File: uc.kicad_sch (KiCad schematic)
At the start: 18 parts, among them J5 490107670612, SW1 DSHP08TSGET, SW2 FSMH, U2 STM32L432KCUx, U8 AD7747, Y1 ECS-.327-7-12RR-TR

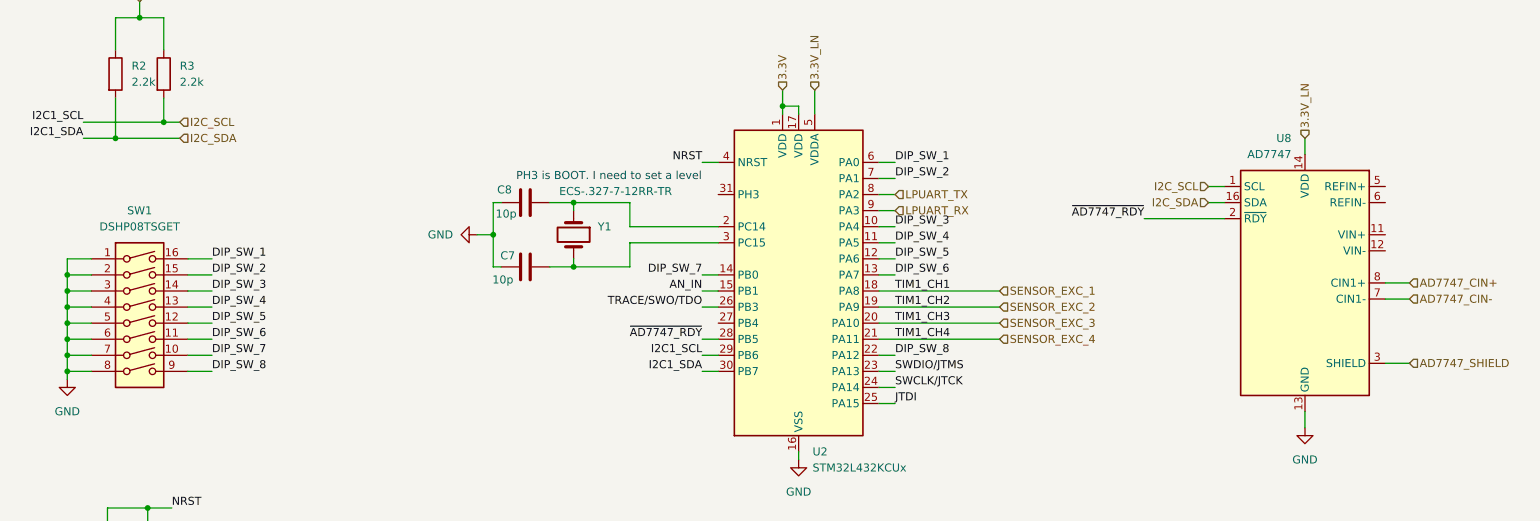
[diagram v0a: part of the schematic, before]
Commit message: rule-check: Fix the ERC errors and warnings
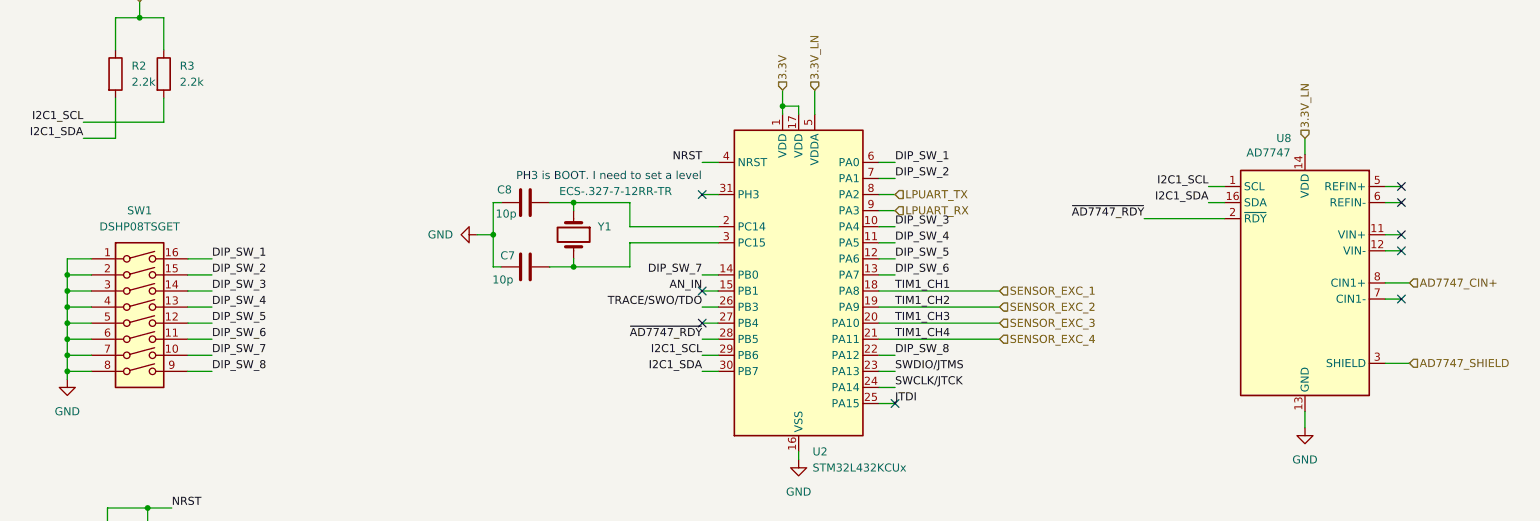
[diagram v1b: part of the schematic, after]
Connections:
- net AD7747_CIN-: no longer names the net of U8.7 (CIN1-)
- net I2C_SCL renamed I2C1_SCL
- net I2C_SDA renamed I2C1_SDA
- no-connect marks 0 -> 9
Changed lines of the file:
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@@
 	)
 	(junction
-		(at 38.1 72.39)
-		(diameter 0)
-		(color 0 0 0 0)
-	)
-	(junction
 		(at 102.87 95.25)
 		(diameter 0)
@@
 	)
 	(junction
-		(at 30.48 74.93)
-		(diameter 0)
-		(color 0 0 0 0)
-	)
-	(junction
 		(at 135.89 69.85)
 		(diameter 0)
@@
 		(color 0 0 0 0)
 	)
+	(no_connect
+		(at 233.68 90.17)
+	)
+	(no_connect
+		(at 123.19 99.06)
+	)
+	(no_connect
+		(at 233.68 82.55)
+	)
+	(no_connect
+		(at 233.68 100.33)
+	)
+	(no_connect
+		(at 123.19 104.14)
+	)
+	(no_connect
+		(at 233.68 92.71)
+	)
+	(no_connect
+		(at 233.68 85.09)
+	)
+	(no_connect
+		(at 153.67 116.84)
+	)
+	(no_connect
+		(at 123.19 83.82)
+	)
 	(wire
 		(pts
@@
 	(wire
 		(pts
+			(xy 231.14 82.55) (xy 233.68 82.55)
+		)
+		(stroke
+			(width 0)
+			(type default)
+		)
+	)
+	(wire
+		(pts
 			(xy 92.71 25.4) (xy 105.41 25.4)
 		)
@@
 	(wire
 		(pts
-			(xy 38.1 72.39) (xy 40.64 72.39)
-		)
-		(stroke
-			(width 0)
-			(type default)
-		)
-	)
-	(wire
-		(pts
 			(xy 45.72 106.68) (xy 41.91 106.68)
 		)
@@
 	(wire
 		(pts
-			(xy 231.14 100.33) (xy 234.95 100.33)
-		)
-		(stroke
-			(width 0)
-			(type default)
-		)
-	)
-	(wire
-		(pts
 			(xy 123.19 111.76) (xy 125.73 111.76)
 		)
@@
 	(wire
 		(pts
-			(xy 30.48 74.93) (xy 40.64 74.93)
+			(xy 231.14 90.17) (xy 233.68 90.17)
 		)
 		(stroke
@@
 	(wire
 		(pts
+			(xy 231.14 85.09) (xy 233.68 85.09)
+		)
+		(stroke
+			(width 0)
+			(type default)
+		)
+	)
+	(wire
+		(pts
 			(xy 34.29 53.34) (xy 34.29 55.88)
 		)
@@
 	(wire
 		(pts
+			(xy 123.19 104.14) (xy 125.73 104.14)
+		)
+		(stroke
+			(width 0)
+			(type default)
+		)
+	)
+	(wire
+		(pts
+			(xy 231.14 92.71) (xy 233.68 92.71)
+		)
+		(stroke
+			(width 0)
+			(type default)
+		)
+	)
+	(wire
+		(pts
 			(xy 151.13 88.9) (xy 153.67 88.9)
 		)
@@
 	(wire
 		(pts
+			(xy 231.14 100.33) (xy 233.68 100.33)
+		)
+		(stroke
+			(width 0)
+			(type default)
+		)
+	)
+	(wire
+		(pts
 			(xy 26.67 104.14) (xy 22.86 104.14)
 		)
@@
 	(wire
 		(pts
+			(xy 123.19 83.82) (xy 125.73 83.82)
+		)
+		(stroke
+			(width 0)
+			(type default)
+		)
+	)
+	(wire
+		(pts
 			(xy 16.51 22.86) (xy 16.51 25.4)
 		)
@@
 		)
 	)
+	(label "I2C1_SDA"
+		(at 203.2 85.09 180)
+		(effects
+			(font
+				(size 1.27 1.27)
+			)
+			(justify right bottom)
+		)
+	)
 	(label "DIP_SW_5"
 		(at 45.72 104.14 0)
@@
 		)
 	)
+	(label "I2C1_SCL"
+		(at 203.2 82.55 180)
+		(effects
+			(font
+				(size 1.27 1.27)
+			)
+			(justify right bottom)
+		)
+	)
 	(label "DIP_SW_8"
 		(at 153.67 109.22 0)
@@
 		)
 	)
-	(hierarchical_label "I2C_SDA"
-		(shape input)
-		(at 40.64 74.93 0)
-		(effects
-			(font
-				(size 1.27 1.27)
-			)
-			(justify left)
-		)
-	)
 	(hierarchical_label "LPUART_RX"
 		(shape input)
@@
 		)
 	)
-	(hierarchical_label "I2C_SDA"
-		(shape input)
-		(at 203.2 85.09 180)
-		(effects
-			(font
-				(size 1.27 1.27)
-			)
-			(justify right)
-		)
-	)
-	(hierarchical_label "I2C_SCL"
-		(shape input)
-		(at 203.2 82.55 180)
-		(effects
-			(font
-				(size 1.27 1.27)
-			)
-			(justify right)
-		)
-	)
-	(hierarchical_label "I2C_SCL"
-		(shape input)
-		(at 40.64 72.39 0)
-		(effects
-			(font
-				(size 1.27 1.27)
-			)
-			(justify left)
-		)
-	)
 	(hierarchical_label "SENSOR_EXC_2"
 		(shape input)
@@
 		)
 	)
-	(hierarchical_label "AD7747_CIN-"
-		(shape input)
-		(at 234.95 100.33 0)
-		(effects
-			(font
-				(size 1.27 1.27)
-			)
-			(justify left)
-		)
-	)
 	(symbol
 		(lib_id "Device:C")
@@
 			)
 		)
+		(property "LCSC" ""
+			(at 138.43 99.06 0)
+			(effects
+				(font
+					(size 1.27 1.27)
+				)
+				(hide yes)
+			)
+		)
 		(pin "21"
 		)
@@
 		)
 		(property "Value" "AD7747"
-			(at 216.2967 77.47 0)
+			(at 216.154 77.216 0)
 			(effects
 				(font
@@
 			)
 		)
-		(property "Datasheet" "https://www.analog.com/media/en/technical-documentation/data-sheets/AD7745_7746.pdf"
+		(property "Datasheet" "https://www.analog.com/media/en/technical-documentation/data-sheets/ad7747.pdf"
 			(at 218.44 97.79 0)
 			(effects
@@
 			)
 		)
+		(property "LCSC" ""
+			(at 218.44 97.79 0)
+			(effects
+				(font
+					(size 1.27 1.27)
+				)
+				(hide yes)
+			)
+		)
 		(pin "10"
 		)
@@
 		(pin "14"
 		)
+		(pin "4"
+		)
 		(instances

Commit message: feature: add three led to notify the status of the device
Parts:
- added D1: KT-0805B Blue, LED_SMD:LED_0805_2012Metric, symbol Device:LED
- added D2: KT-0805R Red, LED_SMD:LED_0805_2012Metric, symbol Device:LED
- added D3: KT-0805G Green, LED_SMD:LED_0805_2012Metric, symbol Device:LED
- added R1, R4: 100, Resistor_SMD:R_0603_1608Metric, symbol Device:R
- added R5: 15, Resistor_SMD:R_0603_1608Metric, symbol Device:R
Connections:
- net GND: now also D1.1 (K), D2.1 (K), D3.1 (K)
- net LED_R: now reaches U2.27 (PB4)
- net LED_R: now also R1.2
- net AN_IN renamed LED_B
- net LED_B: now also R5.1
- net JTDI renamed LED_G
- net LED_G: now also R4.2
- new net: D2.2 (A), R1.1
- new net: D1.2 (A), R5.2
- new net: D3.2 (A), R4.1
- no-connect marks 9 -> 6
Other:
- moved on the sheet: J5

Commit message: chore: fix the naming of connectors sheet file name and the change the path of footprints
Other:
- title: (none) -> ${SHEETNAME}
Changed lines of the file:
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@@
 	(generator_version "9.0")
 	(paper "A4")
+	(title_block
+		(title "${SHEETNAME}")
+	)
 	(text "Keep close to STM32 VDD\n"
 		(exclude_from_sim no)

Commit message: chore: update project to use local footprint and symbols
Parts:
- C10, C11, C13, C14, C15, C16, C19, C7, C8, C9: footprint Capacitor_SMD:C_0603_1608Metric -> footprints:C_0603_1608Metric; symbol Device:C -> symbols:C
- D1, D2, D3: footprint LED_SMD:LED_0805_2012Metric -> footprints:LED_0805_2012Metric; symbol Device:LED -> symbols:LED
- J5: footprint el-ce:Skedd490107670612_2x06_P2.54mm_Debug -> footprints:Skedd490107670612_2x06_P2.54mm_Debug; symbol Connector:Conn_01x06_Socket -> symbols:Conn_01x06_Socket
- R1, R2, R3, R4, R5: footprint Resistor_SMD:R_0603_1608Metric -> footprints:R_0603_1608Metric; symbol Device:R -> symbols:R
- SW1: footprint Button_Switch_SMD:SW_DIP_SPSTx08_Slide_KingTek_DSHP08TJ_W5.25mm_P1.27mm_JPin -> footprints:SW_DIP_SPSTx08_Slide_KingTek_DSHP08TJ_W5.25mm_P1.27mm_JPin; symbol Switch:SW_DIP_x08 -> symbols:SW_DIP_x08
- SW2: footprint Button_Switch_SMD:SW_Tactile_SPST_NO_Straight_CK_PTS636Sx25SMTRLFS -> footprints:SW_Tactile_SPST_NO_Straight_CK_PTS636Sx25SMTRLFS; symbol Switch:SW_Push -> symbols:SW_Push
- U2: footprint Package_DFN_QFN:QFN-32-1EP_5x5mm_P0.5mm_EP3.45x3.45mm -> footprints:QFN-32-1EP_5x5mm_P0.5mm_EP3.45x3.45mm; symbol MCU_ST_STM32L4:STM32L432KCUx -> symbols:STM32L432KCUx
- U8: footprint Package_SO:TSSOP-16_4.4x5mm_P0.65mm -> footprints:TSSOP-16_4.4x5mm_P0.65mm; symbol el_ce-analog_device:AD7747 -> symbols:AD7747
- Y1: footprint Crystal:Crystal_SMD_2012-2Pin_2.0x1.2mm -> footprints:Crystal_SMD_2012-2Pin_2.0x1.2mm; symbol Device:Crystal -> symbols:Crystal
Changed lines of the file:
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@@
 	)
 	(symbol
-		(lib_id "Device:LED")
+		(lib_id "symbols:LED")
 		(at 91.44 165.1 0)
 		(unit 1)
@@
 			)
 		)
-		(property "Footprint" "LED_SMD:LED_0805_2012Metric"
+		(property "Footprint" "footprints:LED_0805_2012Metric"
 			(at 91.44 165.1 0)
 			(effects
@@
 	)
 	(symbol
-		(lib_id "Device:LED")
+		(lib_id "symbols:LED")
 		(at 91.44 153.67 0)
 		(unit 1)
@@
 			)
 		)
-		(property "Footprint" "LED_SMD:LED_0805_2012Metric"
+		(property "Footprint" "footprints:LED_0805_2012Metric"
 			(at 91.44 153.67 0)
 			(effects
@@
 	)
 	(symbol
-		(lib_id "Device:C")
+		(lib_id "symbols:C")
 		(at 105.41 30.48 0)
 		(unit 1)
@@
 			)
 		)
-		(property "Footprint" "Capacitor_SMD:C_0603_1608Metric"
+		(property "Footprint" "footprints:C_0603_1608Metric"
 			(at 106.3752 34.29 0)
 			(effects
@@
 	)
 	(symbol
-		(lib_id "Device:C")
+		(lib_id "symbols:C")
 		(at 95.25 85.09 90)
 		(unit 1)
@@
 			)
 		)
-		(property "Footprint" "Capacitor_SMD:C_0603_1608Metric"
+		(property "Footprint" "footprints:C_0603_1608Metric"
 			(at 99.06 84.1248 0)
 			(effects
@@
 	)
 	(symbol
-		(lib_id "Device:C")
+		(lib_id "symbols:C")
 		(at 40.64 30.48 0)
 		(unit 1)
@@
 			)
 		)
-		(property "Footprint" "Capacitor_SMD:C_0603_1608Metric"
+		(property "Footprint" "footprints:C_0603_1608Metric"
 			(at 41.6052 34.29 0)
 			(effects
@@
 	)
 	(symbol
-		(lib_id "power:GND")
+		(lib_id "symbols:GND")
 		(at 92.71 39.37 0)
 		(unit 1)
@@
 	)
 	(symbol
-		(lib_id "Device:Crystal")
+		(lib_id "symbols:Crystal")
 		(at 102.87 90.17 270)
 		(unit 1)
@@
 			)
 		)
-		(property "Footprint" "Crystal:Crystal_SMD_2012-2Pin_2.0x1.2mm"
+		(property "Footprint" "footprints:Crystal_SMD_2012-2Pin_2.0x1.2mm"
 			(at 102.87 90.17 0)
 			(effects
@@
 	)
 	(symbol
-		(lib_id "Device:C")
+		(lib_id "symbols:C")
 		(at 27.94 30.48 0)
 		(unit 1)
@@
 			)
 		)
-		(property "Footprint" "Capacitor_SMD:C_0603_1608Metric"
+		(property "Footprint" "footprints:C_0603_1608Metric"
 			(at 28.9052 34.29 0)
 			(effects
@@
 	)
 	(symbol
-		(lib_id "Device:R")
+		(lib_id "symbols:R")
 		(at 30.48 64.77 0)
 		(unit 1)
@@
 			)
 		)
-		(property "Footprint" "Resistor_SMD:R_0603_1608Metric"
+		(property "Footprint" "footprints:R_0603_1608Metric"
 			(at 28.702 64.77 90)
 			(effects
@@
 	)
 	(symbol
-		(lib_id "power:GND")
+		(lib_id "symbols:GND")
 		(at 218.44 120.65 0)
 		(unit 1)
@@
 	)
 	(symbol
-		(lib_id "MCU_ST_STM32L4:STM32L432KCUx")
+		(lib_id "symbols:STM32L432KCUx")
 		(at 138.43 99.06 0)
 		(unit 1)
@@
 			)
 		)
-		(property "Footprint" "Package_DFN_QFN:QFN-32-1EP_5x5mm_P0.5mm_EP3.45x3.45mm"
+		(property "Footprint" "footprints:QFN-32-1EP_5x5mm_P0.5mm_EP3.45x3.45mm"
 			(at 128.27 121.92 0)
 			(effects
@@
 			)
 		)
-		(property "Datasheet" "https://www.st.com/resource/en/datasheet/stm32l432kc.pdf"
+		(property "Datasheet" ""
 			(at 138.43 99.06 0)
 			(effects
@@
 			)
 		)
-		(property "Description" "STMicroelectronics Arm Cortex-M4 MCU, 256KB flash, 64KB RAM, 80 MHz, 1.71-3.6V, 26 GPIO, UFQFPN32"
+		(property "Description" ""
 			(at 138.43 99.06 0)
 			(effects
@@
 			)
 		)
-		(property "LCSC" ""
-			(at 138.43 99.06 0)
-			(effects
-				(font
-					(size 1.27 1.27)
-				)
-				(hide yes)
-			)
-		)
 		(pin "21"
 		)
@@
 	)
 	(symbol
-		(lib_id "Device:C")
+		(lib_id "symbols:C")
 		(at 16.51 30.48 0)
 		(unit 1)
@@
 			)
 		)
-		(property "Footprint" "Capacitor_SMD:C_0603_1608Metric"
+		(property "Footprint" "footprints:C_0603_1608Metric"
 			(at 17.4752 34.29 0)
 			(effects
@@
 	)
 	(symbol
-		(lib_id "Device:C")
+		(lib_id "symbols:C")
 		(at 71.12 30.48 0)
 		(unit 1)
@@
 			)
 		)
-		(property "Footprint" "Capacitor_SMD:C_0603_1608Metric"
+		(property "Footprint" "footprints:C_0603_1608Metric"
 			(at 72.0852 34.29 0)
 			(effects
@@
 	)
 	(symbol
-		(lib_id "Device:R")
+		(lib_id "symbols:R")
 		(at 102.87 165.1 90)
 		(unit 1)
@@
 			)
 		)
-		(property "Footprint" "Resistor_SMD:R_0603_1608Metric"
+		(property "Footprint" "footprints:R_0603_1608Metric"
 			(at 102.87 166.878 90)
 			(effects
@@
 	)
 	(symbol
-		(lib_id "Device:C")
+		(lib_id "symbols:C")
 		(at 35.56 140.97 180)
 		(unit 1)
@@
 			)
 		)
-		(property "Footprint" "Capacitor_SMD:C_0603_1608Metric"
+		(property "Footprint" "footprints:C_0603_1608Metric"
 			(at 34.5948 137.16 0)
 			(effects
@@
 	)
 	(symbol
-		(lib_id "power:GND")
+		(lib_id "symbols:GND")
 		(at 22.86 113.03 0)
 		(mirror y)
@@
 	)
 	(symbol
-		(lib_id "Device:R")
+		(lib_id "symbols:R")
 		(at 38.1 64.77 0)
 		(unit 1)
@@
 			)
 		)
-		(property "Footprint" "Resistor_SMD:R_0603_1608Metric"
+		(property "Footprint" "footprints:R_0603_1608Metric"
 			(at 36.322 64.77 90)
 			(effects
@@
 	)
 	(symbol
-		(lib_id "Device:C")
+		(lib_id "symbols:C")
 		(at 95.25 95.25 90)
 		(unit 1)
@@
 			)
 		)
-		(property "Footprint" "Capacitor_SMD:C_0603_1608Metric"
+		(property "Footprint" "footprints:C_0603_1608Metric"
 			(at 99.06 94.2848 0)
 			(effects
@@
 	)
 	(symbol
-		(lib_id "Switch:SW_Push")
+		(lib_id "symbols:SW_Push")
 		(at 29.21 140.97 90)
 		(unit 1)
@@
 			)
 		)
-		(property "Footprint" "Button_Switch_SMD:SW_Tactile_SPST_NO_Straight_CK_PTS636Sx25SMTRLFS"
+		(property "Footprint" "footprints:SW_Tactile_SPST_NO_Straight_CK_PTS636Sx25SMTRLFS"
 			(at 24.13 140.97 0)
 			(effects
@@
 	)
 	(symbol
-		(lib_id "Device:R")
+		(lib_id "symbols:R")
 		(at 102.87 176.53 90)
 		(unit 1)
@@
 			)
 		)
-		(property "Footprint" "Resistor_SMD:R_0603_1608Metric"
+		(property "Footprint" "footprints:R_0603_1608Metric"
 			(at 102.87 178.308 90)
 			(effects
@@
 	)
 	(symbol
-		(lib_id "power:GND")
+		(lib_id "symbols:GND")
 		(at 219.71 46.99 0)
 		(unit 1)
@@
 	)
 	(symbol
-		(lib_id "Device:R")
+		(lib_id "symbols:R")
 		(at 102.87 153.67 270)
 		(mirror x)
@@
 			)
 		)
-		(property "Footprint" "Resistor_SMD:R_0603_1608Metric"
+		(property "Footprint" "footprints:R_0603_1608Metric"
 			(at 102.87 155.448 90)
 			(effects
@@
 	)
 	(symbol
-		(lib_id "Connector:Conn_01x06_Socket")
+		(lib_id "symbols:Conn_01x06_Socket")
 		(at 207.01 39.37 180)
 		(unit 1)
@@
 			)
 		)
-		(property "Footprint" "el-ce:Skedd490107670612_2x06_P2.54mm_Debug"
+		(property "Footprint" "footprints:Skedd490107670612_2x06_P2.54mm_Debug"
 			(at 207.01 39.37 0)
 			(effects
@@
 	)
 	(symbol
-		(lib_id "Device:C")
+		(lib_id "symbols:C")
 		(at 92.71 30.48 0)
 		(unit 1)
@@
 			)
 		)
-		(property "Footprint" "Capacitor_SMD:C_0603_1608Metric"
+		(property "Footprint" "footprints:C_0603_1608Metric"
 			(at 93.6752 34.29 0)
 			(effects
@@
 	)
 	(symbol
-		(lib_id "power:GND")
+		(lib_id "symbols:GND")
 		(at 58.42 39.37 0)
 		(unit 1)
@@
 	)
 	(symbol
-		(lib_id "power:GND")
+		(lib_id "symbols:GND")
 		(at 80.01 182.88 0)
 		(unit 1)
@@
 	)
 	(symbol
-		(lib_id "power:GND")
+		(lib_id "symbols:GND")
 		(at 87.63 90.17 270)
 		(unit 1)
@@
 	)
 	(symbol
-		(lib_id "power:GND")
+		(lib_id "symbols:GND")
 		(at 138.43 125.73 0)
 		(unit 1)
@@
 	)
 	(symbol
-		(lib_id "el_ce-analog_device:AD7747")
+		(lib_id "symbols:AD7747")
 		(at 218.44 97.79 0)
 		(mirror y)
@@
 			)
 		)
-		(property "Footprint" "Package_SO:TSSOP-16_4.4x5mm_P0.65mm"
+		(property "Footprint" "footprints:TSSOP-16_4.4x5mm_P0.65mm"
 			(at 196.85 116.84 0)
 			(effects
@@
 			)
 		)
-		(property "Datasheet" "https://www.analog.com/media/en/technical-documentation/data-sheets/ad7747.pdf"
+		(property "Datasheet" ""
 			(at 218.44 97.79 0)
 			(effects
@@
 			)
 		)
-		(property "Description" "24-bit capacitance-to-digital converter with temperature sensor, TSSOP-16"
+		(property "Description" ""
 			(at 218.44 97.79 0)
 			(effects
@@
 			)
 		)
-		(property "LCSC" ""
-			(at 218.44 97.79 0)
-			(effects
-				(font
-					(size 1.27 1.27)
-				)
-				(hide yes)
-			)
-		)
 		(pin "10"
 		)
@@
 	)
 	(symbol
-		(lib_id "Switch:SW_DIP_x08")
+		(lib_id "symbols:SW_DIP_x08")
 		(at 34.29 104.14 0)
 		(unit 1)
@@
 			)
 		)
-		(property "Footprint" "Button_Switch_SMD:SW_DIP_SPSTx08_Slide_KingTek_DSHP08TJ_W5.25mm_P1.27mm_JPin"
+		(property "Footprint" "footprints:SW_DIP_SPSTx08_Slide_KingTek_DSHP08TJ_W5.25mm_P1.27mm_JPin"
 			(at 34.29 104.14 0)
 			(effects
@@
 	)
 	(symbol
-		(lib_id "power:GND")
+		(lib_id "symbols:GND")
 		(at 35.56 152.4 0)
 		(unit 1)
@@
 	)
 	(symbol
-		(lib_id "Device:LED")
+		(lib_id "symbols:LED")
 		(at 91.44 176.53 0)
 		(unit 1)
@@
 			)
 		)
-		(property "Footprint" "LED_SMD:LED_0805_2012Metric"
+		(property "Footprint" "footprints:LED_0805_2012Metric"
 			(at 91.44 176.53 0)
 			(effects
@@
 	)
 	(symbol
-		(lib_id "power:GND")
+		(lib_id "symbols:GND")
 		(at 27.94 39.37 0)
 		(unit 1)
@@
 	)
 	(symbol
-		(lib_id "Device:C")
+		(lib_id "symbols:C")
 		(at 58.42 30.48 0)
 		(unit 1)
@@
 			)
 		)
-		(property "Footprint" "Capacitor_SMD:C_0603_1608Metric"
+		(property "Footprint" "footprints:C_0603_1608Metric"
 			(at 59.3852 34.29 0)
 			(effects

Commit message: design: Assign LSCS and MPN reference to components
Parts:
- C10, C11, C14, C15, C19: LCSC (none) -> C14663
- C13: LCSC (none) -> C59782
- C16, C9: LCSC (none) -> C19666
- C7, C8: LCSC (none) -> C106245
- D1: value KT-0805B Blue -> ~; MPN (none) -> KT-0805B
- D2: value KT-0805R Red -> ~; MPN (none) -> KT-0805R
- D3: value KT-0805G Green -> ~; MPN (none) -> KT-0805G
- J5: value 490107670612 -> ~; MPN (none) -> 490107670612; now not fitted
- R1, R4: LCSC (none) -> C105588
- R2, R3: LCSC (none) -> C114662
- R5: LCSC (none) -> C128059
- SW1: value DSHP08TSGET -> ~; LCSC (none) -> C40738; MPN (none) -> DSHP08TSGET
- SW2: LCSC (none) -> C36936594
- U2: value STM32L432KCUx -> ~; LCSC (none) -> C2928224; MPN (none) -> STM32L432KBUx
- U8: value AD7747 -> ~; LCSC (none) -> C578507; MPN (none) -> AD7747ARUZ
- Y1: value ECS-.327-7-12RR-TR -> ~; LCSC (none) -> C2450089; MPN (none) -> ECS-.327-7-12RR-TR

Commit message: design: Assign the project version and project company from project variable, which are then substituted during the ci
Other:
- company: (none) -> ${COMPANY}
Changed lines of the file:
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@@
 	(title_block
 		(title "${SHEETNAME}")
+		(rev "${VERSION}")
+		(company "${COMPANY}")
 	)
 	(text "Keep close to STM32 VDD\n"
